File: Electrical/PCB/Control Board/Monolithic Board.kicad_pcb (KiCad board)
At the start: 2 copper layers, 154 x 175 mm, 89 parts, among them J1 ED2627-ND, J10 6posheader, J11 S7038-ND, J12 ED2989-ND-USB, J13 ED1501-ND, J14 ED2989-ND-USB, J15 ED2580-ND, J16 ED2580-ND, J17 ED2744-ND, J18 ED2744-ND, J19 ED2744-ND, J2 ED2627-ND, J20 ED2744-ND, J21 ED2744-ND, J22 ED2744-ND, J23 ED2744-ND, J24 ED2744-ND, J25 ED2744-ND, J26 ED2744-ND, J3 ED2627-ND, J4 ED2627-ND, J5 ED2627-ND, J6 S9175-ND, J7 S9175-ND, J8 6posheader, J9 S7038-ND, M1 Mounting_Holes, T1 test_point, T10 test_point, T11 test_point, T12 test_point, T13 test_point, T14 test_point, T15 test_point, T16 test_point, T17 test_point, T18 test_point, T19 test_point, T2 test_point, T20 test_point, T21 test_point, T3 test_point, T4 test_point, T5 test_point, T6 test_point, T7 test_point, T8 test_point, T9 test_point, U1 LM358-N, U2 LM358-N

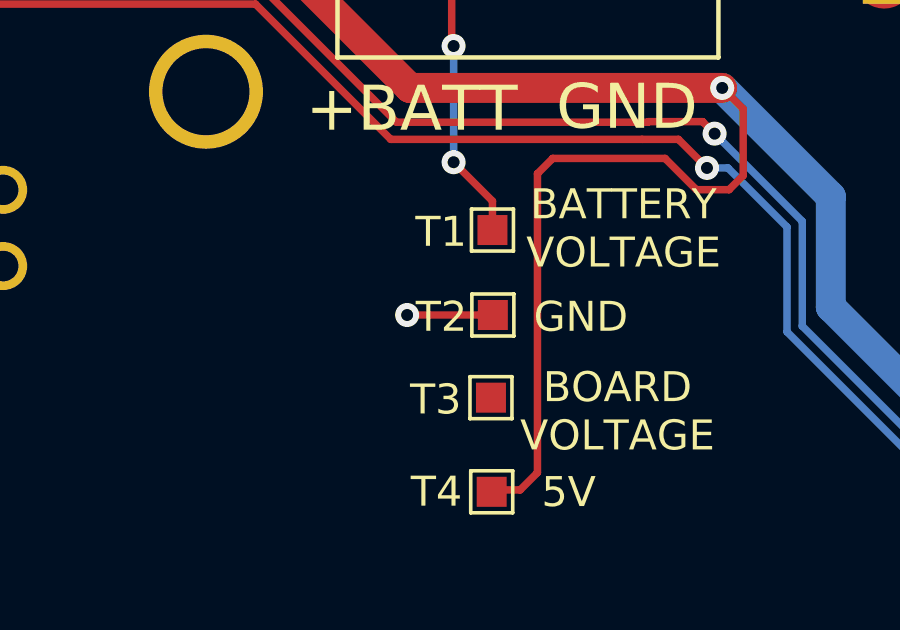
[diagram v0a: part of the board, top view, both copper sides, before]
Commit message: Adding 5.2mAH battery mount. Updating the Encoder mount to have notches for clamping screw tightenting
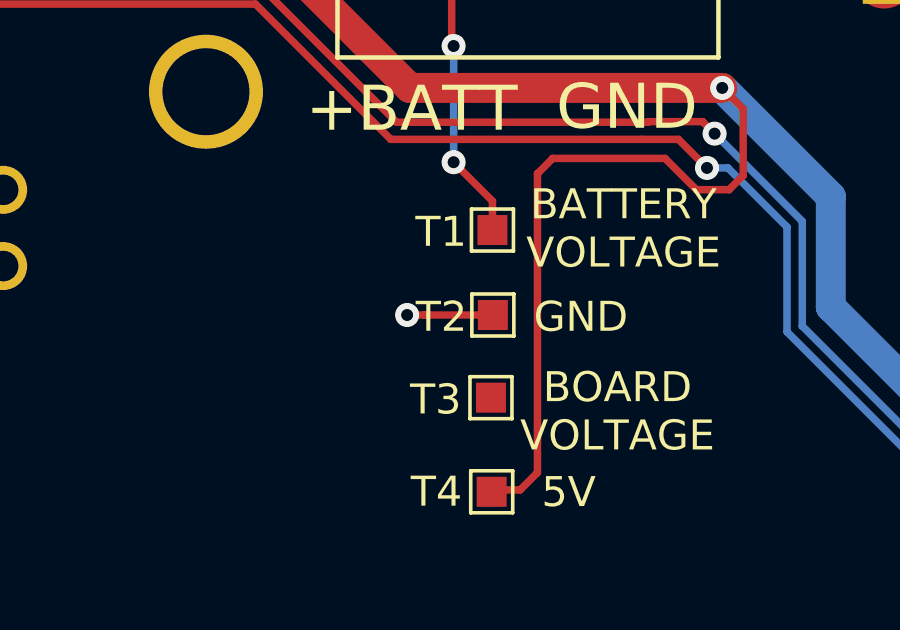
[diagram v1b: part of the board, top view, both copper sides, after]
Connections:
- T2 pad 1: Net-(T2-Pad1) -> GND
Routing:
- net Net-(T2-Pad1): track 2.86 -> 0.00 mm, vias 1 -> 0
- net GND: track 44.8 -> 47.7 mm, vias 1 -> 2
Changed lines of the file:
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@@
     (thickness 1.6)
     (drawings 164)
-    (tracks 1745)
+    (tracks 1746)
     (zones 0)
     (modules 89)
-    (nets 195)
+    (nets 194)
   )
   (page A4)
@@
   (net 191 "Net-(T19-Pad1)")
   (net 192 "Net-(T3-Pad1)")
-  (net 193 "Net-(T2-Pad1)")
-  (net 194 "Net-(T14-Pad1)")
+  (net 193 "Net-(T14-Pad1)")
   (net_class Default "This is the default net class."
     (clearance 0.2)
@@
     (add_net "Net-(T14-Pad1)")
     (add_net "Net-(T19-Pad1)")
-    (add_net "Net-(T2-Pad1)")
     (add_net "Net-(T3-Pad1)")
   )
@@
     )
     (pad 1 smd rect (at 0 0) (size 1 1) (layers F.Cu F.Mask)
-      (net 194 "Net-(T14-Pad1)"))
+      (net 193 "Net-(T14-Pad1)"))
   )
   (module TestPoint:TestPoint_Pad_1.0x1.0mm (layer F.Cu)
@@
     )
     (pad 1 smd rect (at 0 0) (size 1 1) (layers F.Cu F.Mask)
-      (net 193 "Net-(T2-Pad1)"))
+      (net 18 GND))
   )
   (module TestPoint:TestPoint_Pad_1.0x1.0mm (layer F.Cu)
@@
   (segment (start 88.8365 -164.8714) (end 91.2114 -164.8714) (width 2) (layer F.Cu) (net 18))
   (segment (start 135.646234 -7.366) (end 137.414 -7.366) (width 2) (layer F.Cu) (net 18))
-  (via (at 82.2706 -151.3078) (size 0.8) (drill 0.4) (layers F.Cu B.Cu) (net 193))
-  (segment (start 85.1281 -151.3078) (end 82.2706 -151.3078) (width 0.25) (layer F.Cu) (net 193))
-  (via (at 123.698 -36.8935) (size 0.8) (drill 0.4) (layers F.Cu B.Cu) (net 194))
-  (segment (start 121.3485 -37.973) (end 122.6185 -37.973) (width 0.25) (layer F.Cu) (net 194))
-  (segment (start 122.6185 -37.973) (end 123.698 -36.8935) (width 0.25) (layer F.Cu) (net 194))
   (segment (start 73.545 -38.1635) (end 72.5805 -39.128) (width 0.25) (layer F.Cu) (net 18))
   (segment (start 74.295 -38.1635) (end 73.545 -38.1635) (width 0.25) (layer F.Cu) (net 18))
@@
   (segment (start 120.65 -114.3) (end 129.3114 -114.3) (width 0.25) (layer F.Cu) (net 180))
   (segment (start 144.78 -153.252) (end 144.78 -153.39) (width 0.25) (layer B.Cu) (net 185))
+  (via (at 82.2706 -151.3078) (size 0.8) (drill 0.4) (layers F.Cu B.Cu) (net 18))
+  (segment (start 82.836285 -151.3078) (end 85.1281 -151.3078) (width 0.25) (layer F.Cu) (net 18))
+  (segment (start 82.2706 -151.3078) (end 82.836285 -151.3078) (width 0.25) (layer F.Cu) (net 18))
+  (via (at 123.698 -36.8935) (size 0.8) (drill 0.4) (layers F.Cu B.Cu) (net 193))
+  (segment (start 121.3485 -37.973) (end 122.6185 -37.973) (width 0.25) (layer F.Cu) (net 193))
+  (segment (start 122.6185 -37.973) (end 123.698 -36.8935) (width 0.25) (layer F.Cu) (net 193))
   (zone (net 26) (net_name +BATT) (layer F.Cu) (hatch edge 0.508)
     (connect_pads (clearance 0.508))
